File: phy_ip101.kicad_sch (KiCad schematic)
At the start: 48 parts, among them CON3 8P8C, U4 IP101GRI, X1 25MHz

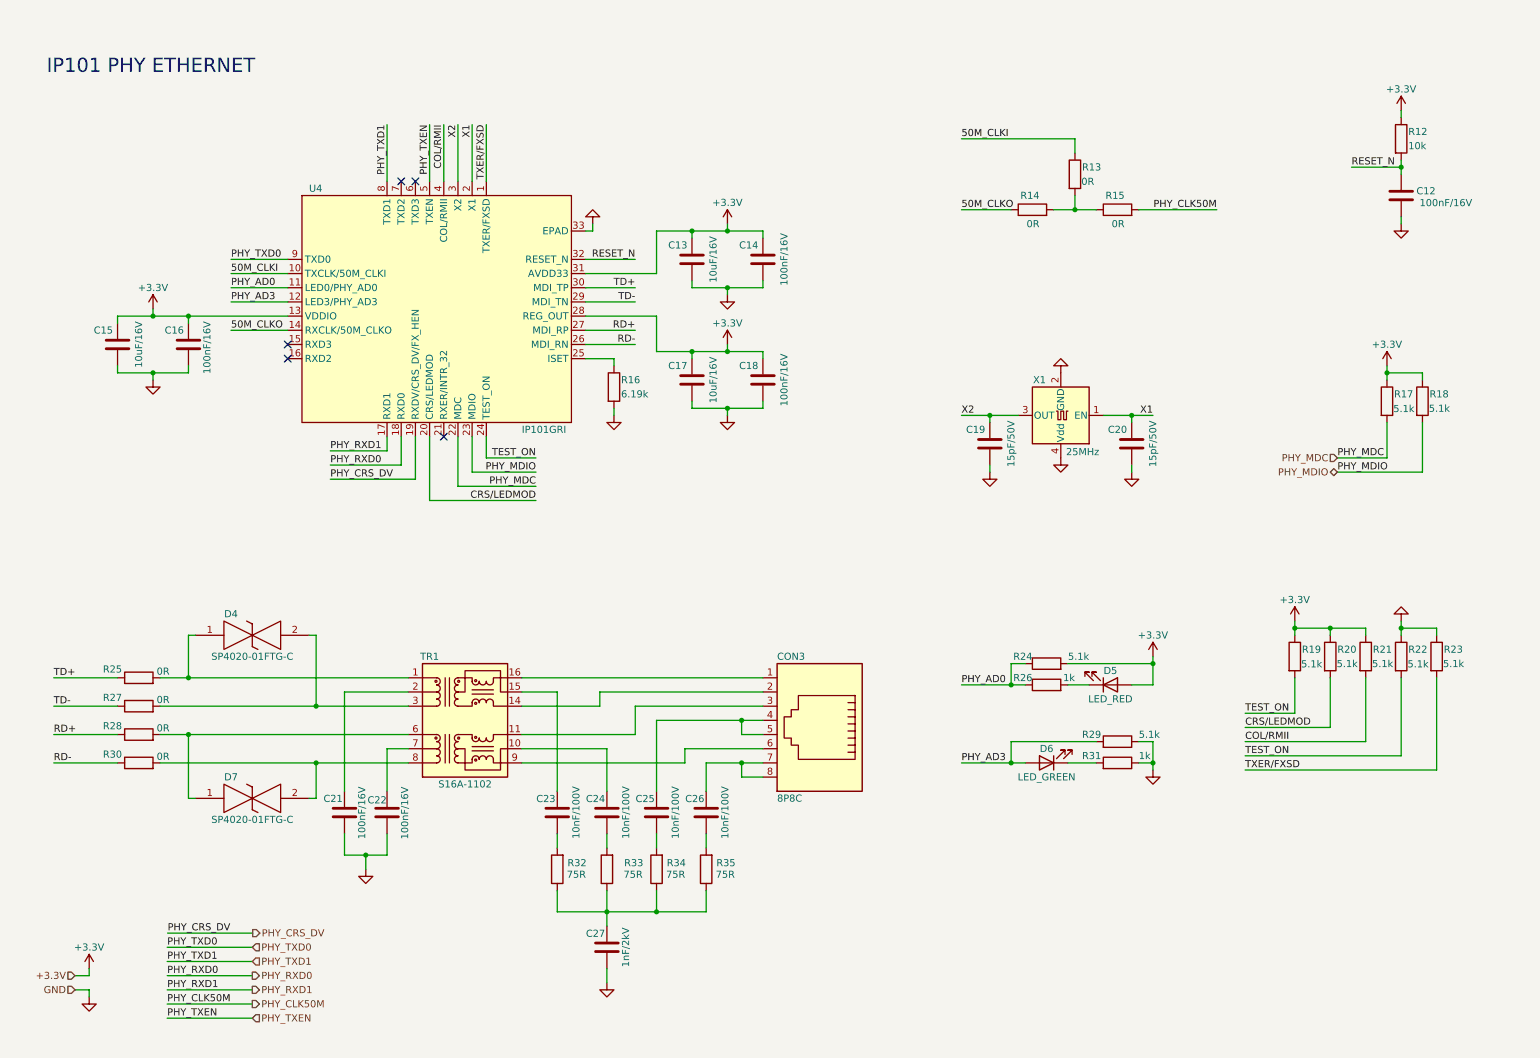
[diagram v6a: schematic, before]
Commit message: Inserido um pino de controle de reset do PHY
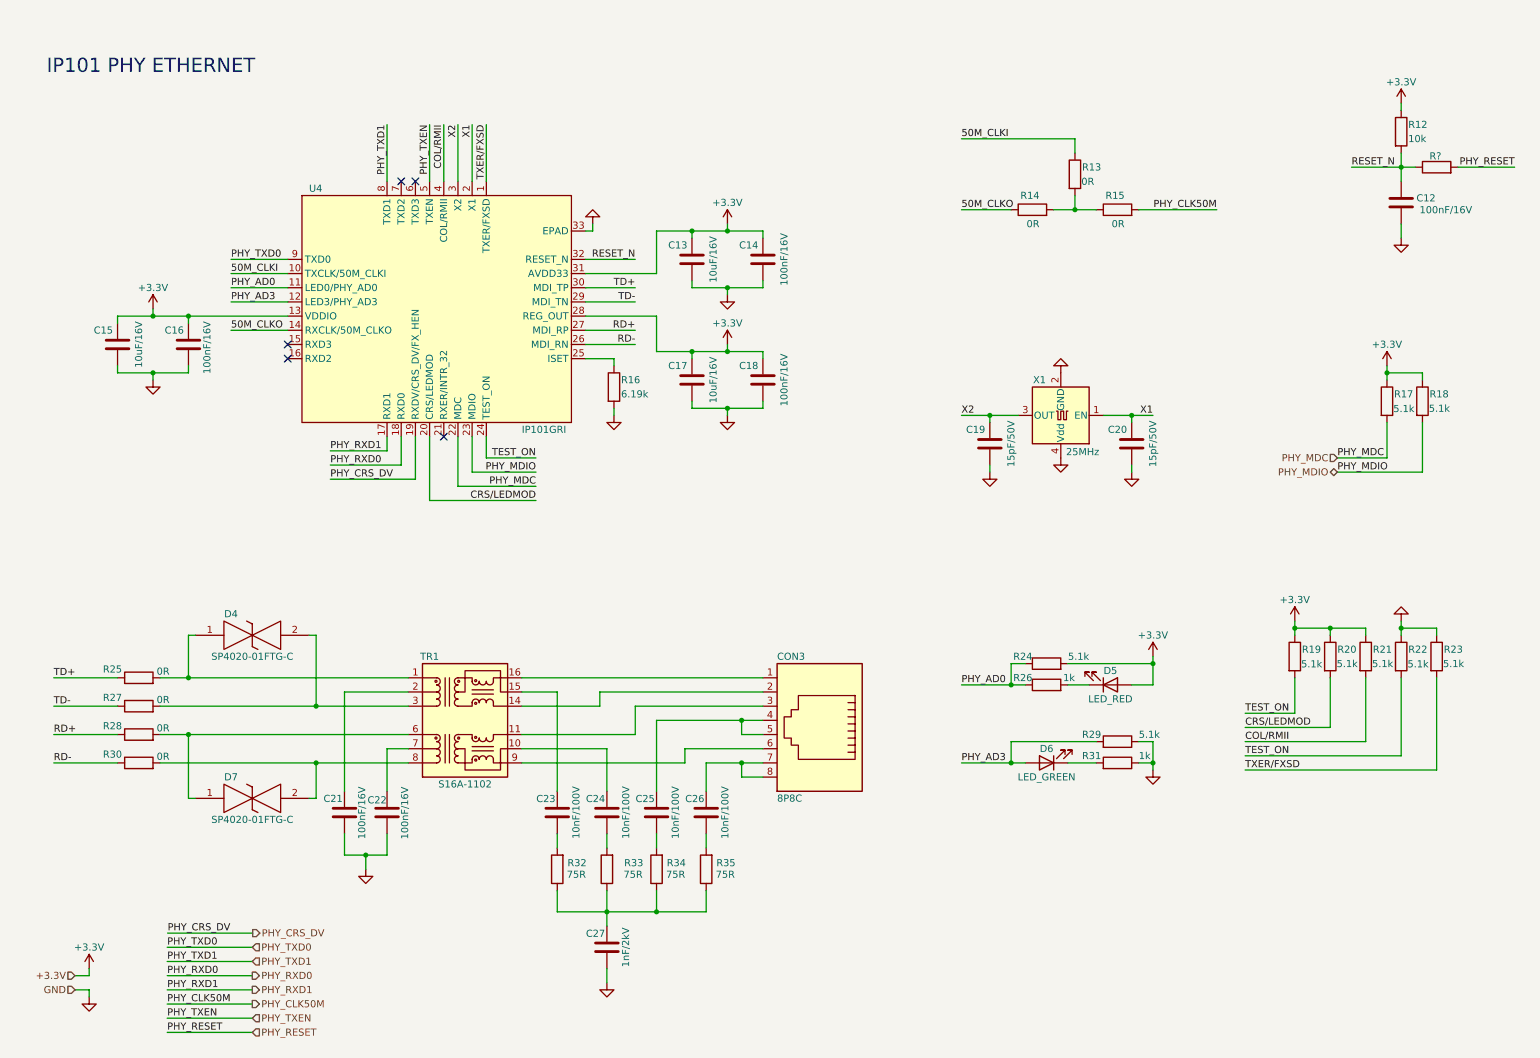
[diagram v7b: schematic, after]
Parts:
- added R?: (no value), Resistor_SMD:R_0603_1608Metric_Pad0.98x0.95mm_HandSolder, symbol Device:R
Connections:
- net RESET_N: now also R?.1
- new net PHY_RESET: R?.2
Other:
- moved on the sheet: C12, R12
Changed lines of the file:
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@@
     (stroke (width 0) (type default) (color 0 0 0 0))
   )
-  (wire (pts (xy 261.62 30.48) (xy 261.62 31.75))
+  (wire (pts (xy 261.62 29.21) (xy 261.62 30.48))
     (stroke (width 0) (type default) (color 0 0 0 0))
   )
@@
     (stroke (width 0) (type default) (color 0 0 0 0))
   )
+  (wire (pts (xy 261.62 40.64) (xy 264.16 40.64))
+    (stroke (width 0) (type default) (color 0 0 0 0))
+  )
   (wire (pts (xy 182.88 35.56) (xy 203.2 35.56))
     (stroke (width 0) (type default) (color 0 0 0 0))
@@
     (stroke (width 0) (type default) (color 0 0 0 0))
   )
+  (wire (pts (xy 271.78 40.64) (xy 281.94 40.64))
+    (stroke (width 0) (type default) (color 0 0 0 0))
+  )
   (wire (pts (xy 31.75 68.58) (xy 31.75 67.31))
     (stroke (width 0) (type default) (color 0 0 0 0))
@@
     (stroke (width 0) (type default) (color 0 0 0 0))
   )
+  (wire (pts (xy 40.64 195.58) (xy 55.88 195.58))
+    (stroke (width 0) (type default) (color 0 0 0 0))
+  )
   (wire (pts (xy 120.65 74.93) (xy 120.65 76.2))
     (stroke (width 0) (type default) (color 0 0 0 0))
@@
     (stroke (width 0) (type default) (color 0 0 0 0))
   )
-  (wire (pts (xy 261.62 39.37) (xy 261.62 40.64))
+  (wire (pts (xy 261.62 38.1) (xy 261.62 40.64))
     (stroke (width 0) (type default) (color 0 0 0 0))
   )
@@
     (stroke (width 0) (type default) (color 0 0 0 0))
   )
-  (wire (pts (xy 261.62 49.53) (xy 261.62 50.8))
+  (wire (pts (xy 261.62 50.8) (xy 261.62 53.34))
     (stroke (width 0) (type default) (color 0 0 0 0))
   )
@@
     (stroke (width 0) (type default) (color 0 0 0 0))
   )
-  (wire (pts (xy 261.62 40.64) (xy 261.62 41.91))
+  (wire (pts (xy 261.62 40.64) (xy 261.62 43.18))
     (stroke (width 0) (type default) (color 0 0 0 0))
   )
@@
     (effects (font (size 1.27 1.27)) (justify left bottom))
   )
+  (label "PHY_RESET" (at 281.94 40.64 180)
+    (effects (font (size 1.27 1.27)) (justify right bottom))
+  )
   (label "RD+" (at 20.32 142.24 0)
     (effects (font (size 1.27 1.27)) (justify left bottom))
@@
   )
   (label "PHY_AD0" (at 182.88 133.35 0)
+    (effects (font (size 1.27 1.27)) (justify left bottom))
+  )
+  (label "PHY_RESET" (at 40.64 195.58 0)
     (effects (font (size 1.27 1.27)) (justify left bottom))
   )
@@
   )
   (hierarchical_label "PHY_RXD1" (shape output) (at 55.88 187.96 0)
+    (effects (font (size 1.27 1.27)) (justify left))
+  )
+  (hierarchical_label "PHY_RESET" (shape input) (at 55.88 195.58 0)
     (effects (font (size 1.27 1.27)) (justify left))
   )
@@
     (pin "1")
   )
-  (symbol (lib_id "power:GND") (at 261.62 50.8 0) (unit 1)
+  (symbol (lib_id "power:GND") (at 261.62 53.34 0) (unit 1)
     (in_bom yes) (on_board yes) (fields_autoplaced)
-    (property "Reference" "#PWR049" (id 0) (at 261.62 57.15 0)
-      (effects (font (size 1.27 1.27)) hide)
-    )
-    (property "Value" "GND" (id 1) (at 261.62 55.88 0)
-      (effects (font (size 1.27 1.27)) hide)
-    )
-    (property "Footprint" "" (id 2) (at 261.62 50.8 0)
-      (effects (font (size 1.27 1.27)) hide)
-    )
-    (property "Datasheet" "" (id 3) (at 261.62 50.8 0)
-      (effects (font (size 1.27 1.27)) hide)
-    )
-    (pin "1")
-  )
-  (symbol (lib_id "Device:R") (at 261.62 35.56 0) (unit 1)
-    (in_bom yes) (on_board yes)
-    (property "Reference" "R12" (id 0) (at 262.89 34.29 0)
-      (effects (font (size 1.27 1.27)) (justify left))
-    )
-    (property "Value" "10k" (id 1) (at 262.89 36.83 0)
-      (effects (font (size 1.27 1.27)) (justify left))
-    )
-    (property "Footprint" "Resistor_SMD:R_0603_1608Metric_Pad0.98x0.95mm_HandSolder" (id 2) (at 259.842 35.56 90)
-      (effects (font (size 1.27 1.27)) hide)
-    )
-    (property "Datasheet" "~" (id 3) (at 261.62 35.56 0)
+    (property "Reference" "#PWR049" (id 0) (at 261.62 59.69 0)
+      (effects (font (size 1.27 1.27)) hide)
+    )
+    (property "Value" "GND" (id 1) (at 261.62 58.42 0)
+      (effects (font (size 1.27 1.27)) hide)
+    )
+    (property "Footprint" "" (id 2) (at 261.62 53.34 0)
+      (effects (font (size 1.27 1.27)) hide)
+    )
+    (property "Datasheet" "" (id 3) (at 261.62 53.34 0)
+      (effects (font (size 1.27 1.27)) hide)
+    )
+    (pin "1")
+  )
+  (symbol (lib_id "Device:R") (at 261.62 34.29 0) (unit 1)
+    (in_bom yes) (on_board yes)
+    (property "Reference" "R12" (id 0) (at 262.89 33.02 0)
+      (effects (font (size 1.27 1.27)) (justify left))
+    )
+    (property "Value" "10k" (id 1) (at 262.89 35.56 0)
+      (effects (font (size 1.27 1.27)) (justify left))
+    )
+    (property "Footprint" "Resistor_SMD:R_0603_1608Metric_Pad0.98x0.95mm_HandSolder" (id 2) (at 259.842 34.29 90)
+      (effects (font (size 1.27 1.27)) hide)
+    )
+    (property "Datasheet" "~" (id 3) (at 261.62 34.29 0)
       (effects (font (size 1.27 1.27)) hide)
     )
@@
     (pin "1")
   )
-  (symbol (lib_id "Device:C") (at 261.62 45.72 180) (unit 1)
-    (in_bom yes) (on_board yes)
-    (property "Reference" "C12" (id 0) (at 266.067 44.9106 0))
-    (property "Value" "100nF/16V" (id 1) (at 269.6269 47.0296 0))
-    (property "Footprint" "Capacitor_SMD:C_0402_1005Metric_Pad0.74x0.62mm_HandSolder" (id 2) (at 260.6548 41.91 0)
-      (effects (font (size 1.27 1.27)) hide)
-    )
-    (property "Datasheet" "~" (id 3) (at 261.62 45.72 0)
+  (symbol (lib_id "Device:C") (at 261.62 46.99 180) (unit 1)
+    (in_bom yes) (on_board yes)
+    (property "Reference" "C12" (id 0) (at 266.067 46.1806 0))
+    (property "Value" "100nF/16V" (id 1) (at 269.6269 48.2996 0))
+    (property "Footprint" "Capacitor_SMD:C_0402_1005Metric_Pad0.74x0.62mm_HandSolder" (id 2) (at 260.6548 43.18 0)
+      (effects (font (size 1.27 1.27)) hide)
+    )
+    (property "Datasheet" "~" (id 3) (at 261.62 46.99 0)
       (effects (font (size 1.27 1.27)) hide)
     )
@@
     (pin "2")
   )
-  (symbol (lib_id "power:+3.3V") (at 261.62 30.48 0) (unit 1)
-    (in_bom yes) (on_board yes)
-    (property "Reference" "#PWR046" (id 0) (at 261.62 34.29 0)
-      (effects (font (size 1.27 1.27)) hide)
-    )
-    (property "Value" "+3.3V" (id 1) (at 261.62 26.67 0))
-    (property "Footprint" "" (id 2) (at 261.62 30.48 0)
-      (effects (font (size 1.27 1.27)) hide)
-    )
-    (property "Datasheet" "" (id 3) (at 261.62 30.48 0)
-      (effects (font (size 1.27 1.27)) hide)
-    )
+  (symbol (lib_id "Device:R") (at 267.97 40.64 90) (unit 1)
+    (in_bom yes) (on_board yes)
+    (property "Reference" "R?" (id 0) (at 268.8175 38.6595 90)
+      (effects (font (size 1.27 1.27)) (justify left))
+    )
+    (property "Value" "" (id 1) (at 269.797 43.0104 90)
+      (effects (font (size 1.27 1.27)) (justify left))
+    )
+    (property "Footprint" "Resistor_SMD:R_0603_1608Metric_Pad0.98x0.95mm_HandSolder" (id 2) (at 267.97 42.418 90)
+      (effects (font (size 1.27 1.27)) hide)
+    )
+    (property "Datasheet" "~" (id 3) (at 267.97 40.64 0)
+      (effects (font (size 1.27 1.27)) hide)
+    )
+    (pin "1")
+    (pin "2")
+  )
+  (symbol (lib_id "power:+3.3V") (at 261.62 29.21 0) (unit 1)
+    (in_bom yes) (on_board yes)
+    (property "Reference" "#PWR046" (id 0) (at 261.62 33.02 0)
+      (effects (font (size 1.27 1.27)) hide)
+    )
+    (property "Value" "+3.3V" (id 1) (at 261.62 25.4 0))
+    (property "Footprint" "" (id 2) (at 261.62 29.21 0)
+      (effects (font (size 1.27 1.27)) hide)
+    )
+    (property "Datasheet" "" (id 3) (at 261.62 29.21 0)
+      (effects (font (size 1.27 1.27)) hide)
+    )

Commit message: Organizado o sheet do PHY ETH
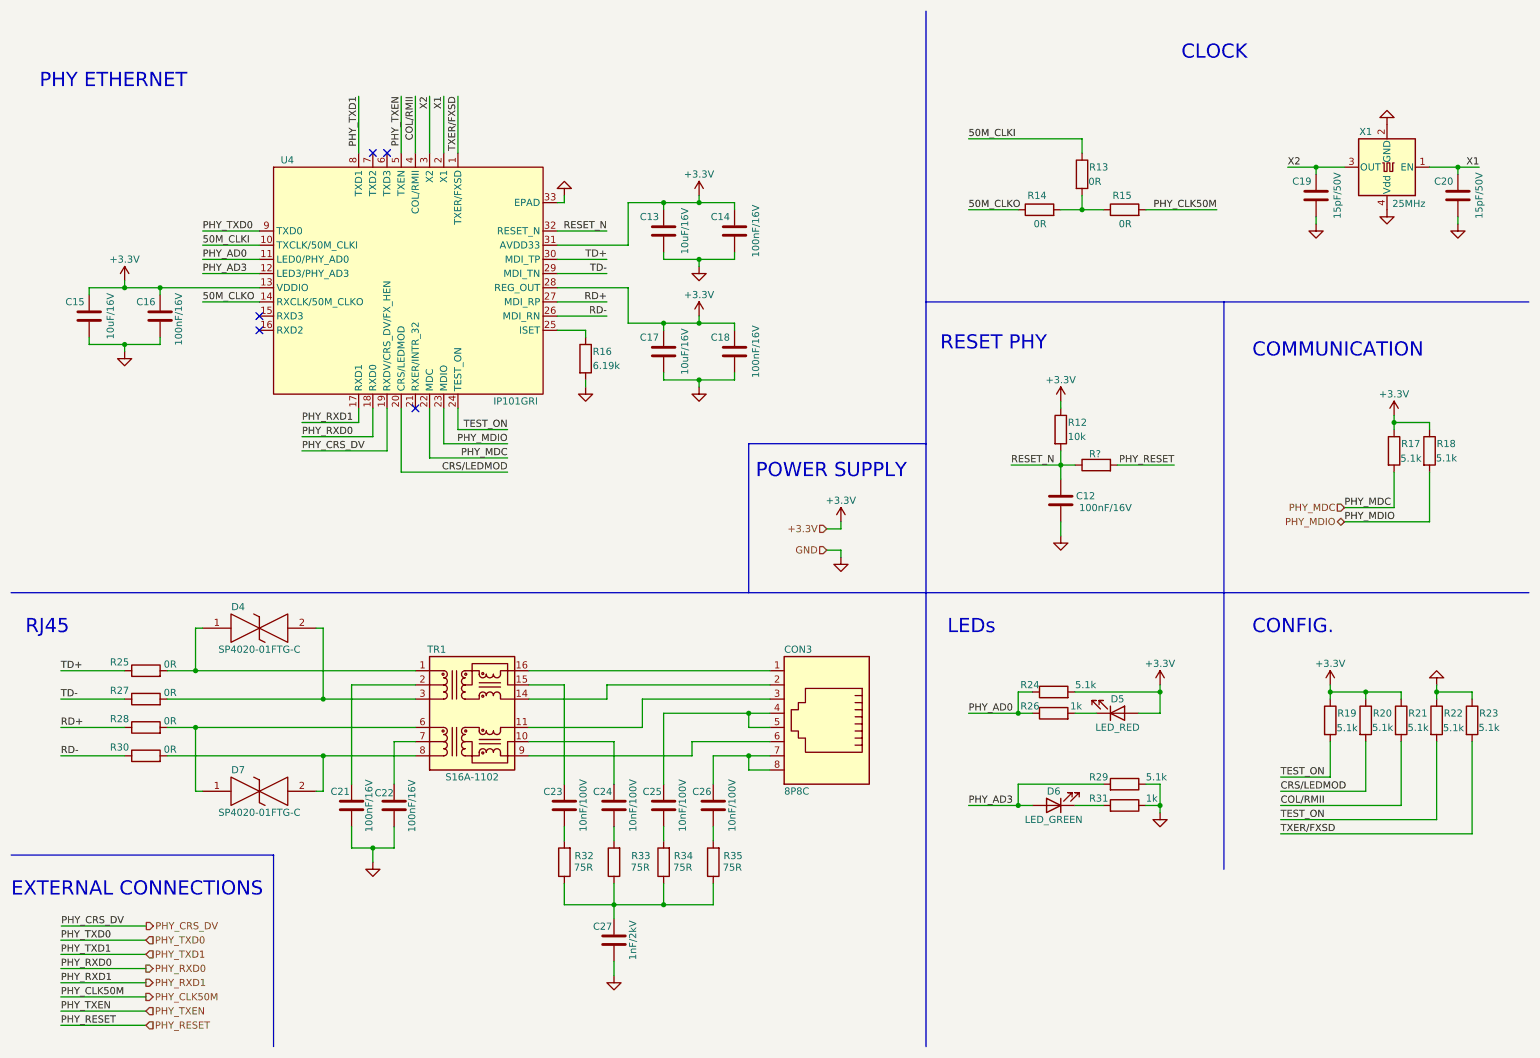
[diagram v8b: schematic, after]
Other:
- note added: "CLOCK"
- note added: "COMMUNICATION"
- note added: "CONFIG."
- note added: "EXTERNAL CONNECTIONS"
- note added: "LEDs"
- note added: "PHY ETHERNET"
- note added: "POWER SUPPLY"
- note added: "RESET PHY"
- note added: "RJ45"
- note removed: "IP101 PHY ETHERNET"
- moved on the sheet: C12, C13, C14, C15, C16, C17, C18, C19, C20, C21, C22, C23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
